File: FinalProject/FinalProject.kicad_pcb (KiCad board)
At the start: 2 copper layers, 50 x 50 mm, 51 parts, among them J1 USB_B_Micro, J2 Conn_01x02, J3 Conn_01x03, J4 Conn_01x02, SW1 SW_Push, U1 RP2040, U2 NCP1117-3.3_SOT223, U3 W25Q128JVS, U4 ABM8-272-T3, U5 MAX98357A, U6 VEML6040

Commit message: fix smt
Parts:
- removed C1, C17, C2: 10μF, Capacitor_SMD:C_0603_1608Metric
- removed C10, C11, C12, C13, C14, C15, C16, C21, C8: 100nF, Capacitor_SMD:C_0603_1608Metric
- removed C18, C19: 0.1μF, Capacitor_SMD:C_0603_1608Metric
- removed C20: 200pF, Capacitor_SMD:C_0603_1608Metric
- removed C9: 1μF, Capacitor_SMD:C_0402_1005Metric
- removed H1, H2, H3, H4: MountingHole, MountingHole:MountingHole_2.7mm_M2.5
- removed J4: Conn_01x02, Connector_PinSocket_2.54mm:PinSocket_1x02_P2.54mm_Vertical
- removed MK1: SPH0645LM4H, Sensor_Audio:Knowles_SPH0645LM4H-6_3.5x2.65mm
- removed R1: 1kΩ, Resistor_SMD:R_0603_1608Metric
- removed R10, R9: 2.2kΩ, Resistor_SMD:R_0603_1608Metric
- removed R11, R12: 150Ω, Resistor_SMD:R_0603_1608Metric
- removed R2: DNF, Resistor_SMD:R_0603_1608Metric
- removed R3, R4: 27Ω, Resistor_SMD:R_0603_1608Metric
- removed R5: 1MΩ, Resistor_SMD:R_0603_1608Metric
- removed R6, R7, R8: 51Ω, Resistor_SMD:R_0603_1608Metric
- removed SW1: SW_Push, Button_Switch_THT:SW_PUSH_1P1T_6x3.5mm_H4.3_APEM_MJTP1243
- removed U6: VEML6040, VEML6040:VISHAY_VEML6040_1.25X2X1
- added C100: 22uF, Capacitor_SMD:C_0603_1608Metric, F.Cu at (74.8, 25.7)
- added C101: 10uF, Capacitor_SMD:C_0603_1608Metric, F.Cu at (74.8, 28.2)
- added C102: 100nF, Capacitor_SMD:C_0603_1608Metric, F.Cu at (74.8, 30.7)
- added C103: 100nF, Capacitor_SMD:C_0603_1608Metric, F.Cu at (74.8, 33.2)
- added C104: 100nF, Capacitor_SMD:C_0603_1608Metric, F.Cu at (74.8, 35.8)
- added C105: 100nF, Capacitor_SMD:C_0603_1608Metric, F.Cu at (74.8, 38.3)
- added C106: 0.1uF, Capacitor_SMD:C_0603_1608Metric, F.Cu at (74.8, 40.8)
- added C22: 0.1uF, Capacitor_SMD:C_0603_1608Metric, F.Cu at (86.6, 77.6)
- added C23: 0.1uF, Capacitor_SMD:C_0603_1608Metric, F.Cu at (86.6, 80.1)
- added C24: 0.1uF, Capacitor_SMD:C_0603_1608Metric, F.Cu at (86.6, 82.6)
- added C25: 0.1uF, Capacitor_SMD:C_0603_1608Metric, F.Cu at (86.6, 85.1)
- added C26: 0.1uF, Capacitor_SMD:C_0603_1608Metric, F.Cu at (90.6, 72.6)
- added C27: 0.1uF, Capacitor_SMD:C_0603_1608Metric, F.Cu at (90.6, 75.1)
- added C28: 0.1uF, Capacitor_SMD:C_0603_1608Metric, F.Cu at (90.6, 77.6)
- added C29: 10uF, Capacitor_SMD:C_0603_1608Metric, F.Cu at (90.6, 80.1)
- added C30: 0.1uF, Capacitor_SMD:C_0603_1608Metric, F.Cu at (90.6, 82.6)
- added C31: 0.1uF, Capacitor_SMD:C_0603_1608Metric, F.Cu at (90.6, 85.1)
- added C32: 0.1uF, Capacitor_SMD:C_0603_1608Metric, F.Cu at (94.6, 72.6)
- added C33: 0.1uF, Capacitor_SMD:C_0603_1608Metric, F.Cu at (94.6, 75.1)
- added C34: 10uF, Capacitor_SMD:C_0603_1608Metric, F.Cu at (94.6, 77.6)
- added C35: 10uF, Capacitor_SMD:C_0603_1608Metric, F.Cu at (94.6, 80.1)
- added C36: 100nF, Capacitor_SMD:C_0603_1608Metric, F.Cu at (62.8, 28.2)
- added C37: 100nF, Capacitor_SMD:C_0603_1608Metric, F.Cu at (62.8, 30.7)
- added C38: 100nF, Capacitor_SMD:C_0603_1608Metric, F.Cu at (62.8, 33.2)
- added C39: 100nF, Capacitor_SMD:C_0603_1608Metric, F.Cu at (62.8, 35.8)
- added C40: 100nF, Capacitor_SMD:C_0603_1608Metric, F.Cu at (62.8, 38.3)
- added C41: 10μF, Capacitor_SMD:C_0603_1608Metric, F.Cu at (62.8, 40.8)
- added C42: 10μF, Capacitor_SMD:C_0603_1608Metric, F.Cu at (62.8, 43.3)
- added C45: 1uF, Capacitor_SMD:C_0603_1608Metric, F.Cu at (94.6, 82.6)
- added C46: 15pF, Capacitor_SMD:C_0402_1005Metric, F.Cu at (74.8, 79.4)
- added C47: 15pF, Capacitor_SMD:C_0402_1005Metric, F.Cu at (74.8, 81.4)
- added C50: 100μF, Capacitor_SMD:C_0603_1608Metric, F.Cu at (59.3, 72.6)
- added C51: 100nF, Capacitor_SMD:C_0603_1608Metric, F.Cu at (59.3, 75.1)
- added C52: 1μF, Capacitor_SMD:C_0402_1005Metric, F.Cu at (74.8, 83.4)
- added C53: 100nF, Capacitor_SMD:C_0603_1608Metric, F.Cu at (59.3, 77.6)
- added C54: 1μF, Capacitor_SMD:C_0402_1005Metric, F.Cu at (74.8, 85.3)
- added C55: 100nF, Capacitor_SMD:C_0603_1608Metric, F.Cu at (59.3, 80.1)
- added C56: 100nF, Capacitor_SMD:C_0603_1608Metric, F.Cu at (59.3, 82.6)
- added C57: 100nF, Capacitor_SMD:C_0603_1608Metric, F.Cu at (59.3, 85.1)
- added C58: 100nF, Capacitor_SMD:C_0603_1608Metric, F.Cu at (59.3, 87.6)
- added C59: 100nF, Capacitor_SMD:C_0603_1608Metric, F.Cu at (63.4, 72.6)
- added C60: 100nF, Capacitor_SMD:C_0603_1608Metric, F.Cu at (63.4, 75.1)
- added C61: 100nF, Capacitor_SMD:C_0603_1608Metric, F.Cu at (63.4, 77.6)
- added C62: 0.1μF, Capacitor_SMD:C_0603_1608Metric, F.Cu at (63.4, 80.1)
- added C63: 200pF, Capacitor_SMD:C_0603_1608Metric, F.Cu at (63.4, 82.6)
- added C64: 100nF, Capacitor_SMD:C_0603_1608Metric, F.Cu at (63.4, 85.1)
- added C65: 10μF, Capacitor_SMD:C_0603_1608Metric, F.Cu at (63.4, 87.6)
- added C66: 0.1μF, Capacitor_SMD:C_0603_1608Metric, F.Cu at (67.4, 72.6)
- added C67: 18pF, Capacitor_SMD:C_0603_1608Metric, F.Cu at (94.6, 85.1)
- added C68: 18pF, Capacitor_SMD:C_0603_1608Metric, F.Cu at (98.6, 72.6)
- added C69: 27pF, Capacitor_SMD:C_0603_1608Metric, F.Cu at (66.8, 20.7)
- added C70: 27pF, Capacitor_SMD:C_0603_1608Metric, F.Cu at (66.8, 23.2)
- added C71: 22nF, Capacitor_SMD:C_0603_1608Metric, F.Cu at (66.8, 25.7)
- added C72: 0.1uF, Capacitor_SMD:C_0603_1608Metric, F.Cu at (98.6, 75.1)
- added C73: 0.1uF, Capacitor_SMD:C_0603_1608Metric, F.Cu at (98.6, 77.6)
- added C74: 0.1uF, Capacitor_SMD:C_0603_1608Metric, F.Cu at (98.6, 80.1)
- added C75: 0.1uF, Capacitor_SMD:C_0603_1608Metric, F.Cu at (66.8, 28.2)
- added C76: 10nF, Capacitor_SMD:C_0603_1608Metric, F.Cu at (66.8, 30.7)
- added C77: 0.1uF, Capacitor_SMD:C_0603_1608Metric, F.Cu at (98.6, 82.6)
- added C78: 0.1uF, Capacitor_SMD:C_0603_1608Metric, F.Cu at (98.6, 85.1)
- added C79: 0.1uF, Capacitor_SMD:C_0603_1608Metric, F.Cu at (66.8, 33.2)
- added C80: 0.1uF, Capacitor_SMD:C_0603_1608Metric, F.Cu at (66.8, 35.8)
- added C81: 0.1uF, Capacitor_SMD:C_0603_1608Metric, F.Cu at (66.8, 38.3)
- added C82: 0.1uF, Capacitor_SMD:C_0603_1608Metric, F.Cu at (66.8, 40.8)
- added C83: 0.1uF, Capacitor_SMD:C_0603_1608Metric, F.Cu at (66.8, 43.3)
- added C84: 0.1uF, Capacitor_SMD:C_0603_1608Metric, F.Cu at (70.8, 20.7)
- added C85: 22nF, Capacitor_SMD:C_0603_1608Metric, F.Cu at (70.8, 23.2)
- added C89: 100nF, Capacitor_SMD:C_0603_1608Metric, F.Cu at (70.8, 25.7)
- added C90: 100nF, Capacitor_SMD:C_0603_1608Metric, F.Cu at (70.8, 28.2)
- added C92: 0.1uF, Capacitor_SMD:C_0603_1608Metric, F.Cu at (70.8, 30.7)
- added C93: 0.1uF, Capacitor_SMD:C_0603_1608Metric, F.Cu at (70.8, 33.2)
- added C94: 0.1uF, Capacitor_SMD:C_0603_1608Metric, F.Cu at (70.8, 35.8)
- added C95: 0.1uF, Capacitor_SMD:C_0603_1608Metric, F.Cu at (70.8, 38.3)
- added C96: 0.1uF, Capacitor_SMD:C_0603_1608Metric, F.Cu at (70.8, 40.8)
- added C97: 0.1uF, Capacitor_SMD:C_0603_1608Metric, F.Cu at (70.8, 43.3)
- added C98: 0.1uF, Capacitor_SMD:C_0603_1608Metric, F.Cu at (74.8, 20.7)
- added C99: 0.1uF, Capacitor_SMD:C_0603_1608Metric, F.Cu at (74.8, 23.2)
- added D3: LED, LED_SMD:LED_0603_1608Metric, F.Cu at (78.7, 99.5)
- added D4: LED, LED_SMD:LED_0603_1608Metric, F.Cu at (78.7, 102.1)
- added FB1: 220 @100MHz, Inductor_SMD:L_0603_1608Metric, F.Cu at (102.6, 72.6)
- added FB2: 220 @100MHz, Inductor_SMD:L_0603_1608Metric, F.Cu at (102.6, 75.1)
- added FB5: 220 @100MHz, Inductor_SMD:L_0603_1608Metric, F.Cu at (102.6, 77.6)
- added FB6: 220 @100MHz, Inductor_SMD:L_0603_1608Metric, F.Cu at (102.6, 80.1)
- added H5: MountingHole, MountingHole:MountingHole_2.7mm_M2.5, F.Cu at (53.9, 74.8)
- added H6: MountingHole, MountingHole:MountingHole_2.7mm_M2.5, F.Cu at (53.9, 81.7)
- added H7: MountingHole, MountingHole:MountingHole_2.7mm_M2.5, F.Cu at (53.9, 88.7)
- added H8: MountingHole, MountingHole:MountingHole_2.7mm_M2.5, F.Cu at (53.9, 95.6)
- added J10: Conn_01x02, Connector_PinSocket_2.54mm:PinSocket_1x02_P2.54mm_Vertical, F.Cu at (80.3, 73.6)
- added J5: ARJM11D7-502-AB-EW2, ARJM11D7-502-AB-EW2:ABRACON_ARJM11D7-502-AB-EW2, F.Cu at (117.1, 31.2)
- added J6: DCJ200-10-A-XX-K_REVA, DCJ200-10-A-XX-K_REVA:GCT_DCJ200-10-A-XX-K_REVA, F.Cu at (131.1, 56.6)
- added J7: Conn_01x02, Connector_PinSocket_2.54mm:PinSocket_1x02_P2.54mm_Vertical, F.Cu at (75.7, 73.6)
- added J9: Conn_01x03, Connector_PinSocket_2.54mm:PinSocket_1x03_P2.54mm_Vertical, F.Cu at (70.0, 91.2)
- added L2: 1uH, Inductor_SMD:L_1008_2520Metric, F.Cu at (65.8, 65.5)
- added MK2: SPH0645LM4H, Sensor_Audio:Knowles_SPH0645LM4H-6_3.5x2.65mm, F.Cu at (74.6, 100.9)
- added Q1: NTTFS5C673NLTAG, KiCad:NVTFS6H854NTAG, F.Cu at (92.0, 41.2)
- added Q2: NTTFS5C673NLTAG, KiCad:NVTFS6H854NTAG, F.Cu at (97.6, 41.2)
- added R16: 90.9K, Resistor_SMD:R_0402_1005Metric, F.Cu at (97.3, 87.4)
- added R17: 10K, Resistor_SMD:R_0402_1005Metric, F.Cu at (97.3, 89.3)
- added R18: 9.53K, Resistor_SMD:R_0402_1005Metric, F.Cu at (97.3, 91.3)
- added R19: 200K, Resistor_SMD:R_0603_1608Metric, F.Cu at (74.8, 43.3)
- added R20: 4.7k, Resistor_SMD:R_0603_1608Metric, F.Cu at (78.8, 20.7)
- added R21: 900K, Resistor_SMD:R_0603_1608Metric, F.Cu at (78.8, 23.2)
- added R22: 4.7K, Resistor_SMD:R_0603_1608Metric, F.Cu at (102.6, 82.6)
- added R23: 1kΩ, Resistor_SMD:R_0603_1608Metric, F.Cu at (67.4, 75.1)
- added R24: DNF, Resistor_SMD:R_0603_1608Metric, F.Cu at (67.4, 77.6)
- added R25: 27Ω, Resistor_SMD:R_0603_1608Metric, F.Cu at (67.4, 80.1)
- added R26: 27Ω, Resistor_SMD:R_0603_1608Metric, F.Cu at (67.4, 82.6)
- added R27: 150Ω, Resistor_SMD:R_0603_1608Metric, F.Cu at (67.4, 85.1)
- added R28: 150Ω, Resistor_SMD:R_0603_1608Metric, F.Cu at (67.4, 87.6)
- added R29: 2.2kΩ, Resistor_SMD:R_0603_1608Metric, F.Cu at (71.4, 72.6)
- added R30: 51Ω, Resistor_SMD:R_0603_1608Metric, F.Cu at (71.4, 75.1)
- added R31: 51Ω, Resistor_SMD:R_0603_1608Metric, F.Cu at (71.4, 77.6)
- added R32: 2.2kΩ, Resistor_SMD:R_0603_1608Metric, F.Cu at (71.4, 80.1)
- added R33: 51Ω, Resistor_SMD:R_0603_1608Metric, F.Cu at (71.4, 82.6)
- added R34: 1MΩ, Resistor_SMD:R_0603_1608Metric, F.Cu at (71.4, 85.1)
- added R35: 4.7K, Resistor_SMD:R_0402_1005Metric, F.Cu at (100.3, 87.4)
- added R36: 4.7K, Resistor_SMD:R_0402_1005Metric, F.Cu at (100.3, 89.3)
- added R37: 4.7K, Resistor_SMD:R_0402_1005Metric, F.Cu at (100.3, 91.3)
- added R38: 4.7K, Resistor_SMD:R_0603_1608Metric, F.Cu at (102.6, 85.1)
- added R39: 2.49K, Resistor_SMD:R_0603_1608Metric, F.Cu at (78.8, 25.7)
- added R40: 470R, Resistor_SMD:R_0603_1608Metric, F.Cu at (78.8, 28.2)
- added R42: 10K, Resistor_SMD:R_0402_1005Metric, F.Cu at (103.2, 87.4)
- added R43: 10K, Resistor_SMD:R_0402_1005Metric, F.Cu at (103.2, 89.3)
- added R44: 25.5K, Resistor_SMD:R_0402_1005Metric, F.Cu at (103.2, 91.3)
- added R45: 11K, Resistor_SMD:R_0603_1608Metric, F.Cu at (78.8, 30.7)
- added R46: 26.1K, Resistor_SMD:R_0603_1608Metric, F.Cu at (78.8, 33.2)
- added SW2: SW_Push, Button_Switch_THT:SW_PUSH_1P1T_6x3.5mm_H4.3_APEM_MJTP1243, F.Cu at (59.2, 98.2)
- added U11: RP2040, Package_DFN_QFN:QFN-56-1EP_7x7mm_P0.4mm_EP3.2x3.2mm, F.Cu at (76.9, 93.5)
- added U12: TUSB8041, Package_DFN_QFN:QFN-64-1EP_9x9mm_P0.5mm_EP6x6mm_ThermalVias, F.Cu at (90.2, 92.0)
- added U13: HD3SS3220IRNHR, HD3SS:RNH0030A, F.Cu at (70.4, 59.8)
- added U14: NCP1117-3.3_SOT223, Package_TO_SOT_SMD:SOT-223-3_TabPin2, F.Cu at (94.4, 61.4)
- added U15: VEML6040, VEML6040:VISHAY_VEML6040_1.25X2X1, F.Cu at (53.2, 100.6)
- added U16: MAX98357A, Package_DFN_QFN:TQFN-16-1EP_3x3mm_P0.5mm_EP1.23x1.23mm, F.Cu at (78.9, 85.5)
- added U8: ABM8-272-T3, ABM8-272-T3:ABM8-272-T3, F.Cu at (79.3, 80.7)
- added U9: W25Q128JVS, Package_SO:SOIC-8_5.3x5.3mm_P1.27mm, F.Cu at (62.5, 92.3)
- added Y2: ABLS-25.000MHZ-B2F-T, ABLS_25_000MHZ_B2F_T:XTAL_ABLS-25.000MHZ-B2F-T, F.Cu at (130.0, 89.2)
- added Y3: ABM3C-24.000MHZ-D4Y-T, footprints1:CRYSTAL_ABM3C_ABR, F.Cu at (99.2, 94.8)
- C3: value 100μF -> 150uF
- C4: value 15pF -> 150uF; footprint Capacitor_SMD:C_0402_1005Metric -> Capacitor_SMD:C_0603_1608Metric
- C5: value 15pF -> 100uF; footprint Capacitor_SMD:C_0402_1005Metric -> Capacitor_SMD:C_0603_1608Metric
- C6: value 1μF -> 100uF; footprint Capacitor_SMD:C_0402_1005Metric -> Capacitor_SMD:C_0603_1608Metric
- C7: value 100nF -> 100uF
- D1, D2: value LED -> SMBJ33CA; footprint LED_SMD:LED_0603_1608Metric -> SMBJ:DIONM5436X261N
- J1: value USB_B_Micro -> 10152803-00011LF; footprint Connector_USB:USB_Micro-B_Amphenol_10103594-0001LF_Horizontal -> 10152803_00011LF:AMPHENOL_10152803-00011LF
- J2: value Conn_01x02 -> GSB4111312HR; footprint Connector_PinSocket_2.54mm:PinSocket_1x02_P2.54mm_Vertical -> GSB4111312HR:AMPHENOL_GSB4111312HR
- J3: value Conn_01x03 -> GSB4111312HR; footprint Connector_PinSocket_2.54mm:PinSocket_1x03_P2.54mm_Vertical -> GSB4111312HR:AMPHENOL_GSB4111312HR
- U1: value RP2040 -> RTL8153B-VB-CG; footprint Package_DFN_QFN:QFN-56-1EP_7x7mm_P0.4mm_EP3.2x3.2mm -> RTL8153B-VB-CG:QFN40P500X500X90-41N
- U2: value NCP1117-3.3_SOT223 -> TPS2561DRCR; footprint Package_TO_SOT_SMD:SOT-223-3_TabPin2 -> footprints:DRC10_2P4X1P65
- U3: value W25Q128JVS -> LM74700; footprint Package_SO:SOIC-8_5.3x5.3mm_P1.27mm -> Package_TO_SOT_SMD:SOT-23-6
- U4: value ABM8-272-T3 -> TPS62902RPJR; footprint ABM8-272-T3:ABM8-272-T3 -> footprints2:QFN_902RPJR_TEX
- U5: value MAX98357A -> LM74700; footprint Package_DFN_QFN:TQFN-16-1EP_3x3mm_P0.5mm_EP1.23x1.23mm -> Package_TO_SOT_SMD:SOT-23-6
- moved J3 109.4 mm to (36.6, 45.6), turned to 0 degrees
- moved C5 87.6 mm to (62.8, 20.7), turned to 0 degrees
- moved C7 84.2 mm to (62.8, 25.7), turned to 0 degrees
- moved J2 78.3 mm to (37.9, 21.9), turned to 0 degrees
- moved C6 75.1 mm to (62.8, 23.2), turned to 0 degrees
- moved U1 65.8 mm to (59.7, 60.9)
- moved U4 65.3 mm to (57.3, 66.5)
- moved U3 63.8 mm to (53.0, 59.6)
- moved U5 62.1 mm to (53.0, 64.3), turned to 0 degrees
- moved D1 47.6 mm to (93.5, 49.0), turned to 0 degrees
- moved U2 44.3 mm to (110.6, 100.7), turned to 0 degrees
- moved D2 43.9 mm to (93.5, 54.5), turned to 0 degrees
- moved C3 36.4 mm to (86.6, 72.6)
- moved C4 34.0 mm to (86.6, 75.1), turned to 0 degrees
- moved J1 25.0 mm to (127.1, 78.1), turned to 0 degrees
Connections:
- C3 pad 1: +3.3V -> Net-(U2-OUT2)
- C4 pad 1: GND -> Net-(U2-OUT1)
- C4 pad 2: /XIN -> GND
- C5 pad 1: GND -> +5V
- C5 pad 2: /XOUT -> GND
- C6 pad 1: +1V1 -> +5V
- C7 pad 1: +1V1 -> /UP_VBUS_DIODE
- D1 pad 2: Net-(D1-A) -> /Power_Supply_5.0
- D2 pad 2: Net-(D2-A) -> /UP_VBUS
- J2 pad 1: GND -> /DN2_VBUS
- J2 pad 2: Net-(J2-Pin_2) -> /DN2_D-
- J3 pad 1: /SWCLK -> /DN3_VBUS
- J3 pad 2: GND -> /DN3_D-
- J3 pad 3: /SWD -> /DN3_D+
- U1 pad 1: +3.3V -> /TD1+
- U1 pad 10: +3.3V -> /TD4-
- U1 pad 11: /GPIO8 -> +3.3V
- U1 pad 12: /GPIO9 -> Net-(U1-U3SSTXN)
- U1 pad 13: unconnected-(U1-GPIO10-Pad13) -> Net-(U1-U3SSTXP)
- U1 pad 14: unconnected-(U1-GPIO11-Pad14) -> +1V1
- U1 pad 15: unconnected-(U1-GPIO12-Pad15) -> /DN1_RXN
- U1 pad 16: unconnected-(U1-GPIO13-Pad16) -> /DN1_RXP
- U1 pad 17: unconnected-(U1-GPIO14-Pad17) -> /DN1_D-
- U1 pad 18: unconnected-(U1-GPIO15-Pad18) -> /DN1_D+
- U1 pad 19: GND -> +1V1
- U1 pad 2: /GPIO0 -> /TD1-
- U1 pad 20: /XIN -> +3.3V
- U1 pad 21: /XOUT -> +5V
- U1 pad 22: +3.3V -> +1V1
- U1 pad 23: +1V1 -> +3.3V
- U1 pad 24: /SWCLK -> /ETH_LED2
- U1 pad 25: /SWD -> GND
- U1 pad 26: /RUN -> unconnected-(U1-VDDREG33-Pad26)
- U1 pad 29: unconnected-(U1-GPIO18-Pad29) -> GND
- U1 pad 3: /GPIO1 -> +1V1
- U1 pad 30: unconnected-(U1-GPIO19-Pad30) -> /ETH_LED1
- U1 pad 32: unconnected-(U1-GPIO21-Pad32) -> /ETH_LED0
- U1 pad 34: unconnected-(U1-GPIO22-Pad34) -> +1V1
- U1 pad 35: unconnected-(U1-GPIO23-Pad35) -> Net-(U1-CKXTAL1)
- U1 pad 36: unconnected-(U1-GPIO24-Pad36) -> GND
- U1 pad 37: unconnected-(U1-GPIO25-Pad37) -> +1V1
- U1 pad 38: unconnected-(U1-GPIO26_ADC0-Pad38) -> Net-(U1-RSET)
- U1 pad 39: unconnected-(U1-GPIO27_ADC1-Pad39) -> +3.3V
- U1 pad 4: /GPIO2 -> /TD2+
- U1 pad 40: unconnected-(U1-GPIO28_ADC2-Pad40) -> +3.3V
- U1 pad 41: unconnected-(U1-GPIO29_ADC3-Pad41) -> GND
- U1 pad 5: /GPIO3 -> /TD2-
- U1 pad 6: /GPIO4 -> /TD3+
- U1 pad 7: /GPIO5 -> /TD3-
- U1 pad 8: /GPIO6 -> +1V1
- U1 pad 9: /GPIO7 -> /TD4+
- U2 pad 2: +3.3V -> +5V
- U3 pad 1: /QSPI_SS -> Net-(U3-VCAP)
- U3 pad 2: /QSPI_SD1 -> GND
- U3 pad 3: /QSPI_SD2 -> /Power_Supply_5.0
- U3 pad 4: GND -> +5V
- U3 pad 5: /QSPI_SD0 -> Net-(Q1-G)
- U3 pad 6: /QSPI_SCLK -> /Power_Supply_5.0
- U4 pad 1: /XIN -> unconnected-(U4-PG-Pad1)
- U4 pad 2: GND -> Net-(U4-SW)
- U4 pad 3: /XOUT -> +1V1
- U5 pad 1: /GPIO0 -> Net-(U5-VCAP)
- U5 pad 3: GND -> /UP_VBUS
- U5 pad 4: Net-(U5-~{SD_MODE}) -> /UP_VBUS_DIODE
- U5 pad 5: unconnected-(U5-NC-Pad5) -> Net-(Q2-G)
- U5 pad 6: unconnected-(U5-NC-Pad6) -> /UP_VBUS
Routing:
- net GND: track 85.9 -> 0.00 mm, vias 19 -> 0
- net +3.3V: track 59.7 -> 0.00 mm, vias 6 -> 0
- net /GPIO7: track 28.3 -> 0.00 mm
- net /GPIO6: track 27.9 -> 0.00 mm, vias 2 -> 0
- net /QSPI_SS: track 26.8 -> 0.00 mm
- net /SWD: track 25.1 -> 0.00 mm
- net /RUN: track 24.3 -> 0.00 mm
- net /SWCLK: track 22.9 -> 0.00 mm
- net +1V1: track 22.8 -> 0.00 mm, vias 3 -> 0
- net Net-(MK1-BCLK): track 21.3 -> 0.00 mm
- net /QSPI_SD1: track 21.1 -> 0.00 mm
- net /QSPI_SD2: track 19.9 -> 0.00 mm
- net /GPIO8: track 16.7 -> 0.00 mm
- net /GPIO9: track 13.7 -> 0.00 mm
- net +5V: track 13.6 -> 0.00 mm, vias 2 -> 0
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- removed copper zone on F.Cu, net +3.3V
- removed copper zone on F.Cu, net +5V
- removed copper zone on B.Cu, net GND
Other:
- board size 50 x 50 mm -> 9.2 x 1.6 mm
- board text removed: "MIC"
- board text removed: "Reset"
- board text removed: "STATUS"
- board text removed: "SWD Debug"
- board text removed: "Speaker"

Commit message: route pi part 1
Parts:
- removed H5, H6, H7, H8: MountingHole, MountingHole:MountingHole_2.7mm_M2.5
- added H1: MountingHole, MountingHole:MountingHole_2.7mm_M2.5, F.Cu at (30.0, 55.0)
- added H2: MountingHole, MountingHole:MountingHole_2.7mm_M2.5, F.Cu at (120.0, 55.0)
- added H3: MountingHole, MountingHole:MountingHole_2.7mm_M2.5, F.Cu at (30.0, 145.0)
- added H4: MountingHole, MountingHole:MountingHole_2.7mm_M2.5, F.Cu at (120.0, 145.0)
- D1, D2: footprint SMBJ:DIONM5436X261N -> SMB:DIONM5436X261N
- FB1, FB2, FB5, FB6: footprint Inductor_SMD:L_0603_1608Metric -> Inductor_SMD:L_0805_2012Metric
- Q1, Q2: footprint KiCad:NVTFS6H854NTAG -> NNTF:NVTFS6H854NTAG
- U2: footprint footprints:DRC10_2P4X1P65 -> TPS2561:DRC10_2P4X1P65
- U4: footprint footprints2:QFN_902RPJR_TEX -> TPS62902:QFN_902RPJR_TEX
- Y3: footprint footprints1:CRYSTAL_ABM3C_ABR -> ABM3C:CRYSTAL_ABM3C_ABR
- moved J1 91.4 mm to (39.5, 52.0), turned to 180 degrees
- moved C69 85.5 mm to (117.3, 89.6)
- moved R20 85.5 mm to (21.9, 84.5)
- moved J6 79.6 mm to (51.5, 56.5), turned to 180 degrees
- moved R21 78.9 mm to (24.5, 80.5)
- moved C70 76.0 mm to (117.1, 80.1)
- moved C5 74.8 mm to (106.0, 81.8)
- moved J10 74.8 mm to (101.0, 145.5), turned to 90 degrees
- moved J7 74.5 mm to (55.3, 145.3), turned to -90 degrees
- moved R38 73.3 mm to (29.3, 87.2), turned to 90 degrees
- moved C38 72.6 mm to (17.2, 89.8)
- moved C39 72.6 mm to (17.2, 92.3)
- moved C37 72.6 mm to (17.2, 87.2)
- moved C40 72.6 mm to (17.2, 94.8)
- moved C68 70.8 mm to (31.3, 94.7), turned to -90 degrees
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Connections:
- net Net-(U11-USB_DM) renamed /RP2040/USB_DN
- net Net-(U11-USB_DP) renamed /RP2040/USB_DP
- C70 pad 1: GND -> Net-(U1-CKXTAL2)
- U1 pad 36: GND -> Net-(U1-CKXTAL2)
- U11 pad 2: /RP2040/GPIO0 -> unconnected-(U11-GPIO0-Pad2)
- U11 pad 29: unconnected-(U11-GPIO18-Pad29) -> /RP2040/GPIO7
- U11 pad 3: /RP2040/GPIO1 -> unconnected-(U11-GPIO1-Pad3)
- U11 pad 30: unconnected-(U11-GPIO19-Pad30) -> /RP2040/GPIO6
- U11 pad 31: unconnected-(U11-GPIO20-Pad31) -> /RP2040/GPIO5
- U11 pad 32: unconnected-(U11-GPIO21-Pad32) -> /RP2040/GPIO3
- U11 pad 34: unconnected-(U11-GPIO22-Pad34) -> /RP2040/GPIO4
- U11 pad 35: unconnected-(U11-GPIO23-Pad35) -> /RP2040/GPIO0
- U11 pad 36: unconnected-(U11-GPIO24-Pad36) -> /RP2040/GPIO1
- U11 pad 37: unconnected-(U11-GPIO25-Pad37) -> /RP2040/GPIO2
- U11 pad 4: /RP2040/GPIO2 -> unconnected-(U11-GPIO2-Pad4)
- U11 pad 5: /RP2040/GPIO3 -> unconnected-(U11-GPIO3-Pad5)
- U11 pad 6: /RP2040/GPIO4 -> unconnected-(U11-GPIO4-Pad6)
- U11 pad 7: /RP2040/GPIO5 -> unconnected-(U11-GPIO5-Pad7)
- U11 pad 8: /RP2040/GPIO6 -> unconnected-(U11-GPIO6-Pad8)
- U11 pad 9: /RP2040/GPIO7 -> unconnected-(U11-GPIO7-Pad9)
- Y2 pad 2: GND -> Net-(U1-CKXTAL2)
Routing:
- net /RP2040/GPIO2: track 0.00 -> 43.3 mm
- net /RP2040/GPIO0: track 0.00 -> 42.8 mm
- net /RP2040/GPIO1: track 0.00 -> 42.4 mm
- net /RP2040/GPIO7: track 0.00 -> 37.6 mm
- net +3.3V: track 0.00 -> 35.7 mm
- net /RP2040/GPIO6: track 0.00 -> 35.6 mm
- net /RP2040/GPIO4: track 0.00 -> 33.9 mm
- net Net-(J7-Pin_2): track 0.00 -> 28.0 mm, vias 0 -> 1
- net /RP2040/RUN: track 0.00 -> 26.0 mm
- net /RP2040/QSPI_SS: track 0.00 -> 25.5 mm
- net /RP2040/GPIO8: track 0.00 -> 24.2 mm
- net /RP2040/SWD: track 0.00 -> 23.9 mm
- net /RP2040/GPIO3: track 0.00 -> 22.7 mm
- net Net-(J10-Pin_1): track 0.00 -> 22.6 mm
- net /RP2040/SWCLK: track 0.00 -> 22.2 mm
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- added copper zone on F.Cu, net /Power_Supply_5.0
- added copper zone on F.Cu, net GND
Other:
- board size 9.2 x 1.6 mm -> 100 x 100 mm

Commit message: checkpoint
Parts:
- removed C36, C37, C38, C39, C40: 100nF, Capacitor_SMD:C_0603_1608Metric
- removed R19: 200K, Resistor_SMD:R_0603_1608Metric
- removed R20: 4.7k, Resistor_SMD:R_0603_1608Metric
- removed R21: 900K, Resistor_SMD:R_0603_1608Metric
- removed U13: HD3SS3220IRNHR, HD3SS:RNH0030A
- J1: value 10152803-00011LF -> GSB4111312HR; footprint 10152803_00011LF:AMPHENOL_10152803-00011LF -> GSB4111312HR:AMPHENOL_GSB4111312HR
- moved C27 67.9 mm to (92.2, 86.5), turned to 180 degrees
- moved C26 66.9 mm to (92.2, 88.0), turned to 180 degrees
- moved C25 65.8 mm to (92.2, 91.5), turned to 180 degrees
- moved C24 60.5 mm to (87.8, 96.5), turned to 90 degrees
- moved C23 58.0 mm to (85.2, 96.5), turned to 90 degrees
- moved C22 56.7 mm to (83.8, 96.5), turned to 90 degrees
- moved C29 55.1 mm to (78.8, 90.2)
- moved C28 54.2 mm to (76.5, 86.0), turned to -90 degrees
- moved U2 53.3 mm to (120.8, 85.8), turned to 90 degrees
- moved C31 52.4 mm to (88.0, 83.8)
- moved C30 51.7 mm to (89.5, 96.5), turned to 90 degrees
- moved R16 49.6 mm to (81.9, 81.7), turned to -90 degrees
- moved C3 47.6 mm to (122.1, 80.8)
- moved FB6 46.8 mm to (120.9, 76.7), turned to 90 degrees
- moved R42 46.3 mm to (119.0, 83.0), turned to 180 degrees
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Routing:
- net Net-(C30-Pad2): track 0.00 -> 41.4 mm
- net +3.3V: track 35.7 -> 59.3 mm
- net Net-(C22-Pad2): track 0.00 -> 23.2 mm
- net +5V: track 19.7 -> 36.7 mm
- net Net-(U12-XI): track 0.00 -> 15.9 mm
- net Net-(U12-XO): track 0.00 -> 12.3 mm
- net Net-(J7-Pin_2): track 28.0 -> 40.3 mm
- net /Power_Supply_5.0: track 18.9 -> 30.4 mm
- net Net-(U2-OUT2): track 0.00 -> 7.15 mm
- net Net-(U2-OUT1): track 0.00 -> 7.09 mm
- net Net-(U2-ILIM): track 0.00 -> 2.59 mm
- net Net-(U11-VREG_VOUT): track 7.56 -> 10.1 mm
- net Net-(Q1-G): track 2.69 -> 4.78 mm
- net Net-(U12-USB_R1): track 0.00 -> 2.05 mm
- net +1V1: track 5.62 -> 7.34 mm
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- removed copper zone on F.Cu, net GND

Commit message: checkpoint 2
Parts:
- moved FB6 34.4 mm to (86.4, 76.0), turned to 180 degrees
- moved C74 33.4 mm to (89.0, 74.8), turned to -90 degrees
- moved FB5 32.5 mm to (86.4, 78.0), turned to 180 degrees
- moved C3 32.2 mm to (90.5, 74.7), turned to 90 degrees
- moved R44 31.7 mm to (91.8, 74.3), turned to -90 degrees
- moved R43 31.0 mm to (92.8, 74.3), turned to -90 degrees
- moved C4 30.1 mm to (89.0, 77.8), turned to -90 degrees
- moved C73 28.8 mm to (90.5, 77.8), turned to 90 degrees
- moved U2 27.0 mm to (95.5, 76.1), turned to 180 degrees
- moved R42 26.8 mm to (92.8, 77.8), turned to -90 degrees
- moved C84 21.1 mm to (117.8, 104.8), turned to 180 degrees
- moved C83 19.5 mm to (117.8, 106.2), turned to 180 degrees
- moved C96 16.3 mm to (115.5, 104.2), turned to -90 degrees
- moved C64 15.3 mm to (96.8, 124.8), turned to -90 degrees
- moved C89 13.8 mm to (91.0, 110.2)
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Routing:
- net +3.3V: track 59.3 -> 208.6 mm, vias 0 -> 11
- net +1V1: track 7.34 -> 107.7 mm, vias 0 -> 2
- net Net-(C22-Pad2): track 23.2 -> 85.0 mm, vias 0 -> 5
- net Net-(C30-Pad2): track 41.4 -> 100.9 mm
- net +5V: track 36.7 -> 90.4 mm, vias 0 -> 4
- net /UP_VBUS_DIODE: track 0.00 -> 31.5 mm
- net /USB HUB/BATEN3: track 0.00 -> 23.7 mm, vias 0 -> 2
- net /UP_VBUS: track 0.00 -> 21.5 mm
- net /USB HUB/BATEN2: track 0.00 -> 20.9 mm, vias 0 -> 2
- net Net-(U1-RSET): track 1.74 -> 14.7 mm, vias 0 -> 2
- net Net-(U12-GRSTz): track 0.00 -> 6.64 mm
- net Net-(U1-CKXTAL2): track 9.52 -> 13.8 mm
- net Net-(U1-CKXTAL1): track 18.3 -> 22.4 mm
- net Net-(U12-USB_VBUS): track 0.00 -> 3.80 mm
- net Net-(U12-TEST): track 1.67 -> 3.51 mm
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- added copper zone on F.Cu, net +3.3V
- added copper zone on F.Cu, net +5V

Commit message: help
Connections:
- net Net-(C22-Pad2) renamed /USB HUB/USB_FB_1.1V
- net Net-(C30-Pad2) renamed /USB HUB/USB_FB_3.3V
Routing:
- net +3.3V: track 208.6 -> 106.4 mm, vias 11 -> 14
- net +1V1: track 107.7 -> 11.0 mm, vias 2 -> 3
- net /USB HUB/USB_FB_3.3V: track 100.9 -> 20.4 mm, vias 0 -> 5
- net /USB HUB/USB_FB_1.1V: track 85.0 -> 31.8 mm, vias 5 -> 4
- net +5V: track 90.4 -> 38.3 mm
- net /USB HUB/BATEN3: track 23.7 -> 12.6 mm, vias 2 -> 0
- net /USB HUB/BATEN2: track 20.9 -> 11.8 mm, vias 2 -> 0
- net GND: track 0.00 -> 1.20 mm, vias 0 -> 1
- net (no net): vias 0 -> 1
- added copper zone on F.Cu, net +1V1
- added copper zone on In1.Cu, net +3.3V
- added copper zone on In2.Cu, net +5V
- added copper zone on F.Cu, net /USB HUB/USB_FB_1.1V
- added copper zone on In1.Cu, net /USB HUB/USB_FB_3.3V
- added copper zone on B.Cu, net GND
- removed copper zone on F.Cu, net +3.3V
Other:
- copper layers 2 -> 4

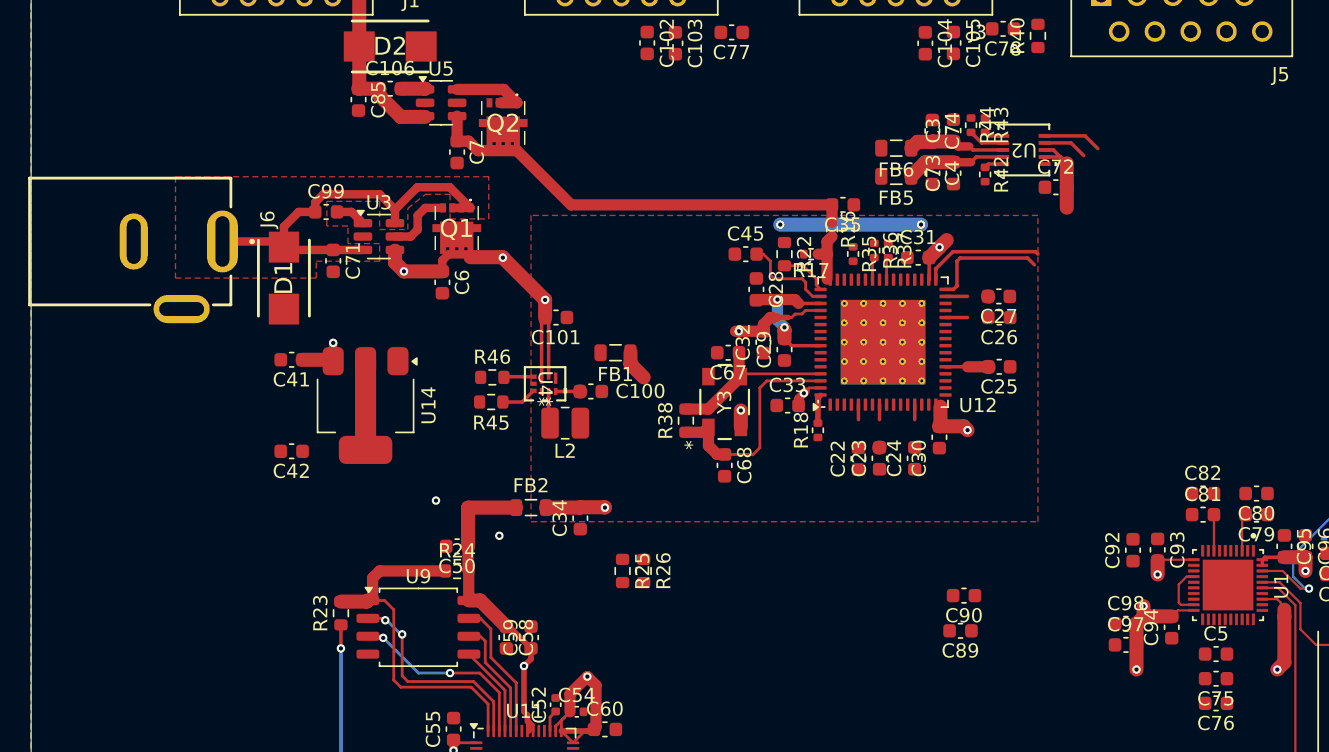
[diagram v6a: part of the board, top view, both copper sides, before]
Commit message: update big capacitors footprint to use bigger than 0603
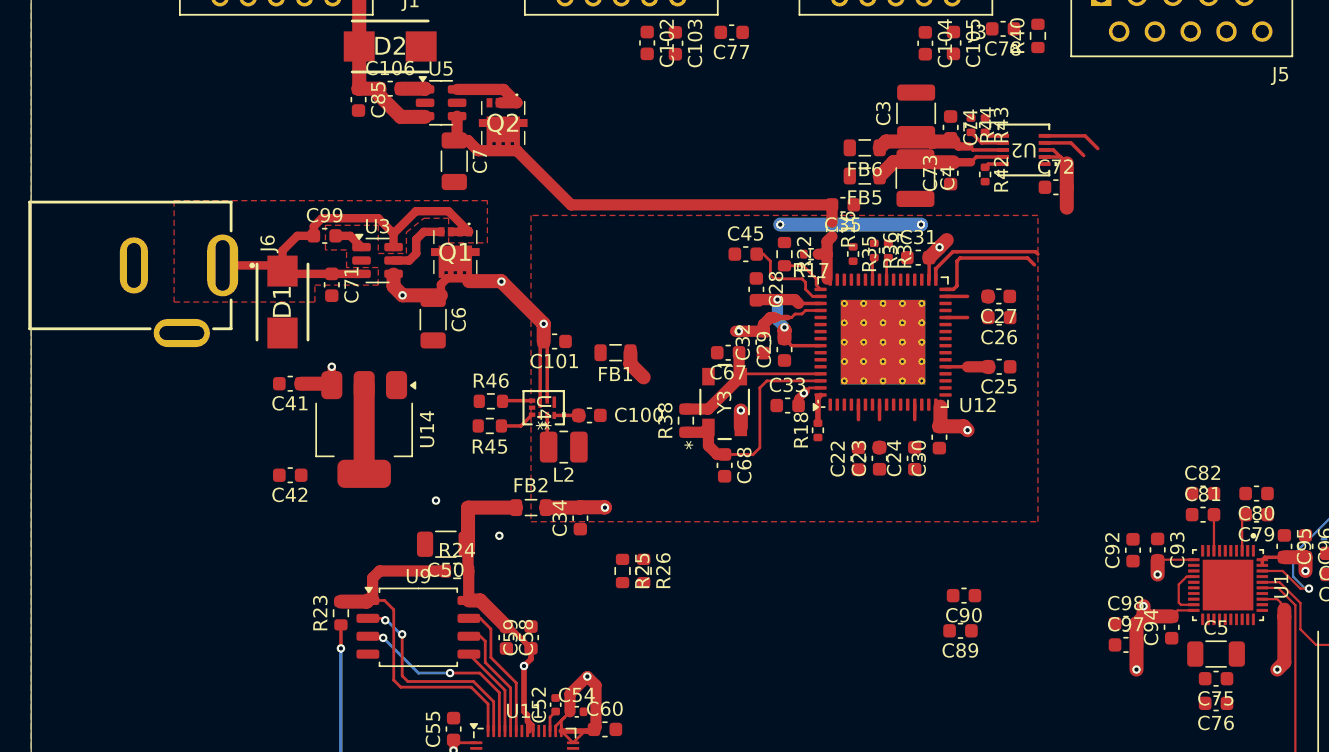
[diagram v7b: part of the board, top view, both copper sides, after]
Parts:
- C3, C4: footprint Capacitor_SMD:C_0603_1608Metric -> Capacitor_SMD:C_1210_3225Metric
- C5, C50, C6, C7: footprint Capacitor_SMD:C_0603_1608Metric -> Capacitor_SMD:C_1206_3216Metric
- moved C3 2.92 mm to (87.8, 73.5)
- moved C6 2.73 mm to (53.5, 88.2)
- moved FB5 2.24 mm to (84.2, 78.0)
- moved FB6 2.24 mm to (84.2, 76.0)
- moved C101 1.70 mm to (62.2, 89.7)
- moved C41 1.70 mm to (43.4, 92.7)
- moved C42 1.70 mm to (43.4, 99.2)
- moved C71 1.70 mm to (46.4, 85.7)
- moved C99 1.70 mm to (45.9, 82.2)
- moved D1 1.70 mm to (42.9, 86.9)
- moved R46 1.70 mm to (57.6, 94.0)
- moved U14 1.70 mm to (48.6, 96.0)
- moved U3 1.70 mm to (49.6, 84.0)
- moved U4 1.70 mm to (61.4, 94.4)
- moved C100 1.70 mm to (64.7, 95.0)
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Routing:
- net Net-(U2-OUT2): track 7.15 -> 9.39 mm
- net Net-(U2-OUT1): track 7.09 -> 9.34 mm
